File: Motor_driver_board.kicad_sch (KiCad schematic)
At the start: 0 parts

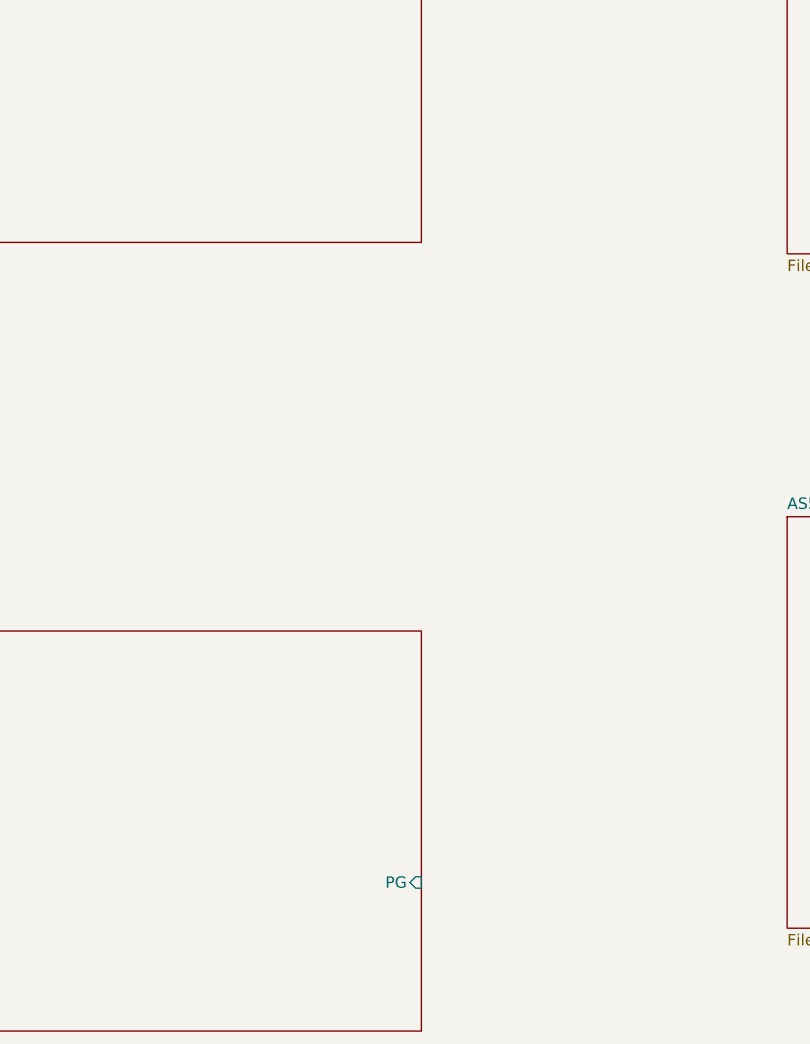
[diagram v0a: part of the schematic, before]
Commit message: Added additional Labels
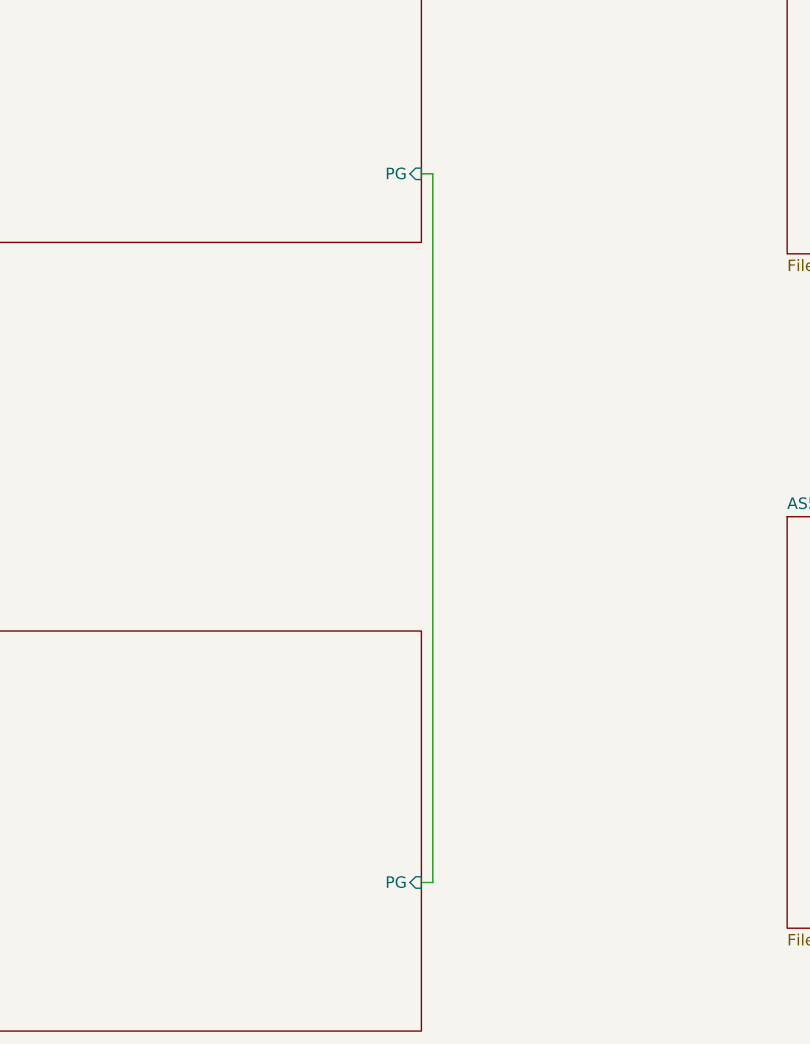
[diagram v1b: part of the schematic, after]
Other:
- sheet ESP32_S3_mini ports: added PG; removed none
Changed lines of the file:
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@@
 	(generator_version "9.0")
 	(paper "A4")
+	(wire
+		(pts
+			(xy 111.76 149.86) (xy 113.03 149.86)
+		)
+		(stroke
+			(width 0)
+			(type default)
+		)
+	)
+	(wire
+		(pts
+			(xy 113.03 149.86) (xy 113.03 71.12)
+		)
+		(stroke
+			(width 0)
+			(type default)
+		)
+	)
+	(wire
+		(pts
+			(xy 111.76 71.12) (xy 113.03 71.12)
+		)
+		(stroke
+			(width 0)
+			(type default)
+		)
+	)
 	(sheet
 		(at 35.56 121.92)
@@
 			)
 		)
+		(pin "PG" input
+			(at 111.76 71.12 0)
+			(effects
+				(font
+					(size 1.27 1.27)
+				)
+				(justify right)
+			)
+		)

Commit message: Layed out PCB
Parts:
- added FID1, FID2, FID3: Fiducial, Fiducial:Fiducial_1mm_Mask2mm, symbol Mechanical:Fiducial
- added H1, H2, H3, H4: MountingHole, MountingHole:MountingHole_3.2mm_M3, symbol Mechanical:MountingHole
